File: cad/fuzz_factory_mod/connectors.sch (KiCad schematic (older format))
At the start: 6 parts

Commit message: Continued schematic
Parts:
- added R? (x2): 1M, symbol Device:R
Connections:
- net at K?.1 (+): now also D?.3 (common)
- net at K?.10 (R2): now also K?.3 (R1)
- net at K?.12 (-): now also D?.1 (A), Q?.3 (C)
- net AUDIO_OUT_CONN: now reaches K?.4 (C1)
- net AUDIO_OUT_CONN: now also R?.2
- net AUDIO_FX_OUT: now reaches K?.5 (T1)
- net AUDIO_FX_IN: now reaches K?.8 (T2)
- net AUDIO_IN_CONN: now reaches K?.9 (C2)
- net AUDIO_IN_CONN: now also R?.2
- net BYPASS_CMD: now reaches Q?.1 (B)
- net GNDPWR: now reaches Q?.2 (E)
- new net GNDA: R?.1, R?.1
- no-connect marks 0 -> 1
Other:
- moved on the sheet: D?, K?, Q?
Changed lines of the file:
@@
 $Descr A4 11693 8268
 encoding utf-8
-Sheet 4 5
+Sheet 5 6
 Title ""
 Date ""
@@
 L flax_lib:EE2-5NU K?
 U 1 1 5DE5A46A
-P 5550 3150
-F 0 "K?" H 5550 3681 50  0000 C CNN
-F 1 "EE2-5NU" H 5550 3590 50  0000 C CNN
-F 2 "" H 5550 3150 50  0000 C CNN
-F 3 "" H 5550 3150 50  0000 C CNN
-	1    5550 3150
+P 7900 4650
+F 0 "K?" H 7900 5181 50  0000 C CNN
+F 1 "EE2-5NU" H 7900 5090 50  0000 C CNN
+F 2 "" H 7900 4650 50  0000 C CNN
+F 3 "" H 7900 4650 50  0000 C CNN
+	1    7900 4650
 	1    0    0    -1
 $EndComp
@@
 L Transistor_BJT:DTC114Y Q?
 U 1 1 5DE5E2B7
-P 4800 4300
-F 0 "Q?" H 4988 4346 50  0000 L CNN
-F 1 "DTC114Y" H 4988 4255 50  0000 L CNN
-F 2 "" H 4800 4300 50  0001 L CNN
-F 3 "" H 4800 4300 50  0001 L CNN
-	1    4800 4300
+P 6400 5300
+F 0 "Q?" H 6588 5346 50  0000 L CNN
+F 1 "DTC114Y" H 6588 5255 50  0000 L CNN
+F 2 "" H 6400 5300 50  0001 L CNN
+F 3 "" H 6400 5300 50  0001 L CNN
+	1    6400 5300
 	1    0    0    -1
 $EndComp
@@
 L flax_lib:BAV23S D?
 U 1 1 5DE5F68B
-P 5850 4300
-F 0 "D?" V 5896 4379 50  0000 L CNN
-F 1 "BAV23S" V 5805 4379 50  0000 L CNN
-F 2 "" H 5850 4300 50  0001 C CNN
-F 3 "" H 5850 4300 50  0001 C CNN
-	1    5850 4300
-	0    -1   -1   0
+P 7400 5300
+F 0 "D?" V 7446 5379 50  0000 L CNN
+F 1 "BAV23S" V 7355 5379 50  0000 L CNN
+F 2 "" H 7400 5300 50  0001 C CNN
+F 3 "" H 7400 5300 50  0001 C CNN
+	1    7400 5300
+	1    0    0    1
 $EndComp
 $Comp
@@
 	1    0    0    -1
 $EndComp
+Wire Wire Line
+	8300 4600 8500 4600
+Wire Wire Line
+	8500 4600 8500 4300
+Wire Wire Line
+	8500 4300 8300 4300
+$Comp
+L power:GNDPWR #PWR?
+U 1 1 5E049671
+P 6500 5600
+F 0 "#PWR?" H 6500 5400 50  0001 C CNN
+F 1 "GNDPWR" H 6504 5446 50  0000 C CNN
+F 2 "" H 6500 5550 50  0001 C CNN
+F 3 "" H 6500 5550 50  0001 C CNN
+	1    6500 5600
+	1    0    0    -1
+$EndComp
+Wire Wire Line
+	6500 5500 6500 5600
+Wire Wire Line
+	6500 5000 6500 5100
+Wire Wire Line
+	6500 5000 7000 5000
+Wire Wire Line
+	7500 4900 7400 4900
+Wire Wire Line
+	7400 4900 7400 5100
+Wire Wire Line
+	7100 5300 7000 5300
+Wire Wire Line
+	7000 5300 7000 5000
+Connection ~ 7000 5000
+Wire Wire Line
+	7000 5000 7500 5000
+NoConn ~ 7700 5300
+Text HLabel 6000 5300 0    50   Input ~ 0
+BYPASS_CMD
+Wire Wire Line
+	6150 5300 6000 5300
+Text HLabel 7100 4400 0    50   Input ~ 0
+AUDIO_IN_CONN
+Text HLabel 7100 4700 0    50   Input ~ 0
+AUDIO_OUT_CONN
+$Comp
+L Device:R R?
+U 1 1 5E0563EF
+P 7400 4150
+F 0 "R?" H 7470 4196 50  0000 L CNN
+F 1 "1M" H 7470 4105 50  0000 L CNN
+F 2 "" V 7330 4150 50  0001 C CNN
+F 3 "~" H 7400 4150 50  0001 C CNN
+	1    7400 4150
+	1    0    0    -1
+$EndComp
+$Comp
+L Device:R R?
+U 1 1 5E056DB3
+P 7200 4150
+F 0 "R?" V 7300 4250 50  0000 R CNN
+F 1 "1M" V 7300 4100 50  0000 R CNN
+F 2 "" V 7130 4150 50  0001 C CNN
+F 3 "~" H 7200 4150 50  0001 C CNN
+	1    7200 4150
+	-1   0    0    -1
+$EndComp
+Wire Wire Line
+	7100 4400 7200 4400
+Wire Wire Line
+	7100 4700 7400 4700
+Wire Wire Line
+	7400 4300 7400 4700
+Connection ~ 7400 4700
+Wire Wire Line
+	7400 4700 7500 4700
+Wire Wire Line
+	7200 4300 7200 4400
+Connection ~ 7200 4400
+Wire Wire Line
+	7200 4400 7500 4400
+$Comp
+L power:GNDA #PWR?
+U 1 1 5E058766
+P 7400 3900
+F 0 "#PWR?" H 7400 3650 50  0001 C CNN
+F 1 "GNDA" H 7405 3727 50  0000 C CNN
+F 2 "" H 7400 3900 50  0001 C CNN
+F 3 "" H 7400 3900 50  0001 C CNN
+	1    7400 3900
+	-1   0    0    1
+$EndComp
+$Comp
+L power:GNDA #PWR?
+U 1 1 5E059243
+P 7200 3900
+F 0 "#PWR?" H 7200 3650 50  0001 C CNN
+F 1 "GNDA" H 7205 3727 50  0000 C CNN
+F 2 "" H 7200 3900 50  0001 C CNN
+F 3 "" H 7200 3900 50  0001 C CNN
+	1    7200 3900
+	-1   0    0    1
+$EndComp
+Wire Wire Line
+	7400 3900 7400 4000
+Wire Wire Line
+	7200 3900 7200 4000
+Text HLabel 8700 4500 2    50   Input ~ 0
+AUDIO_FX_IN
+Text HLabel 8700 4800 2    50   Input ~ 0
+AUDIO_FX_OUT
+Wire Wire Line
+	8700 4800 8300 4800
+Wire Wire Line
+	8300 4500 8700 4500
 $EndSCHEMATC

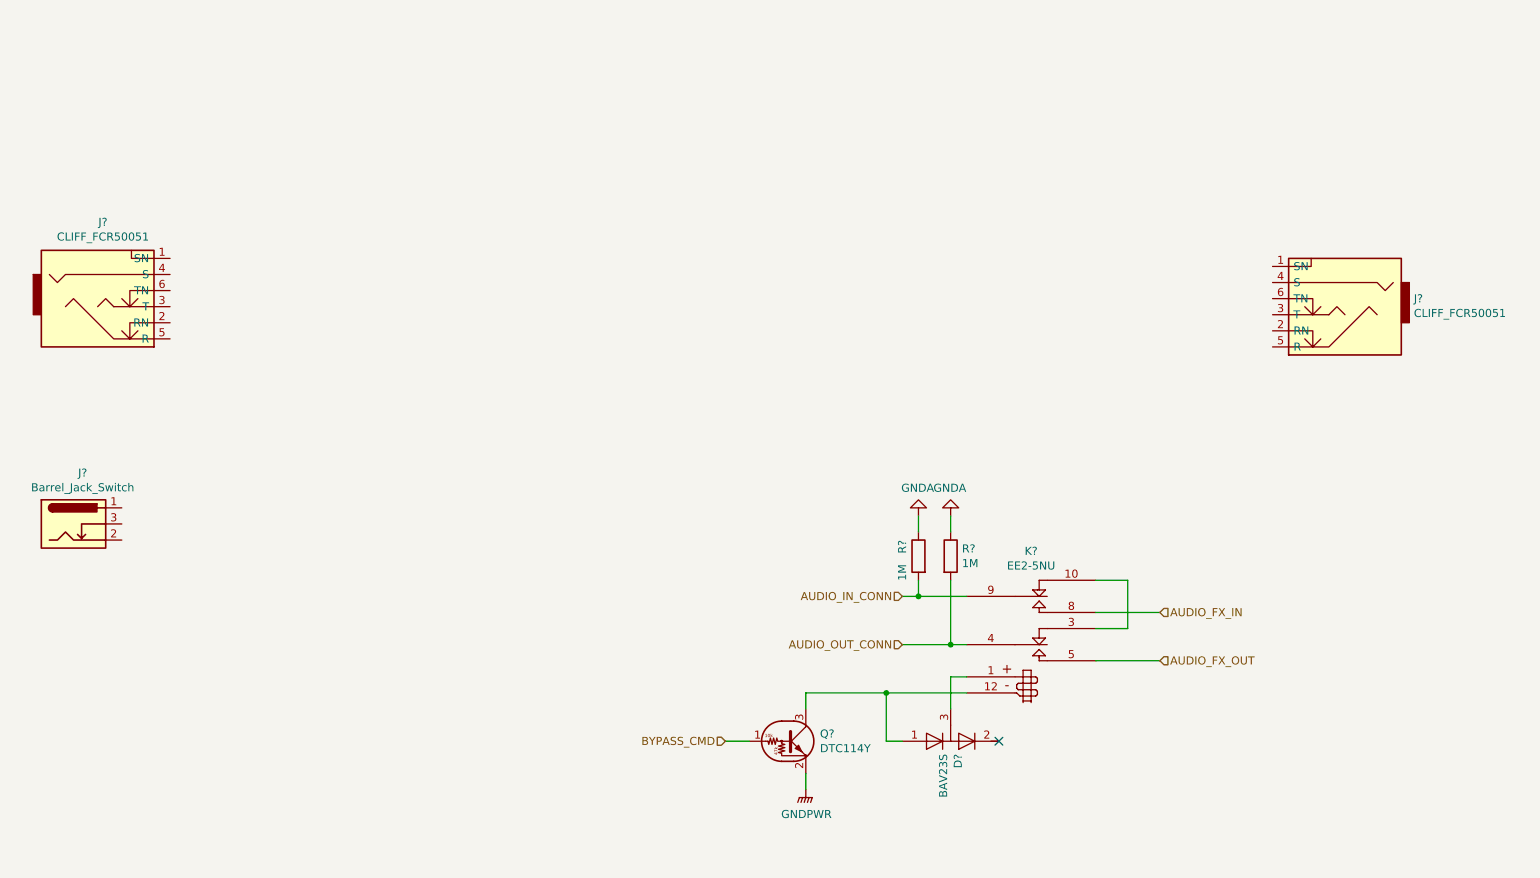
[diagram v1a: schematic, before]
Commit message: Continued schematic.
Added PSU and interface from tremolo project.
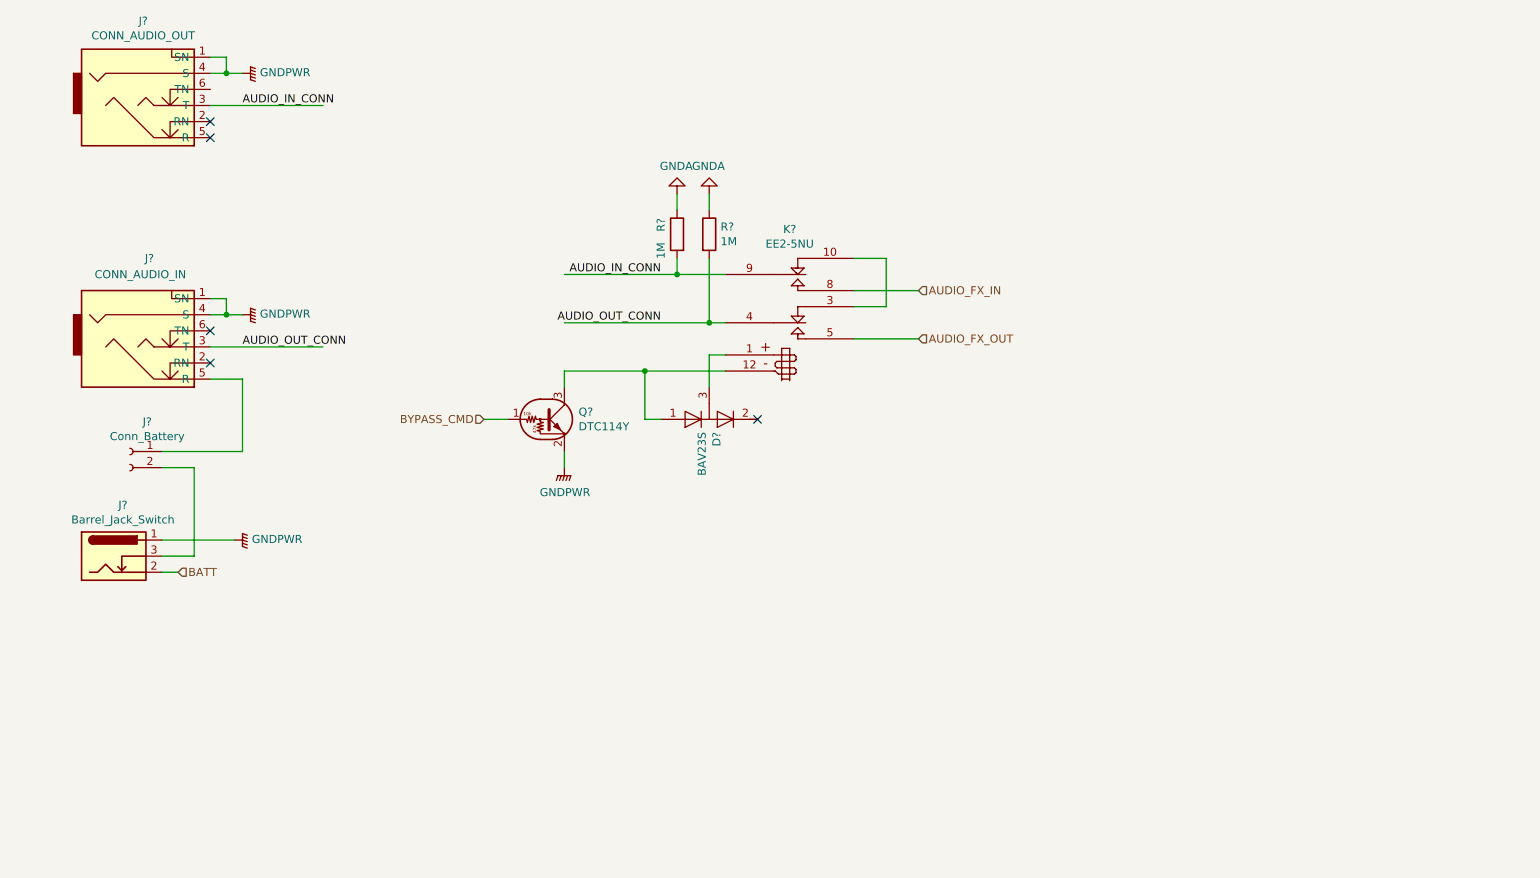
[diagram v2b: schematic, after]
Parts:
- added J?: Conn_Battery, symbol Connector:Conn_01x02_Female
- J?: value CLIFF_FCR50051 -> CONN_AUDIO_OUT
- J?: value CLIFF_FCR50051 -> CONN_AUDIO_IN
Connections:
- net labels added: BATT
- wire segments 22 -> 40
- no-connect marks 1 -> 5
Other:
- moved on the sheet: D?, J?, K?, Q?, R?

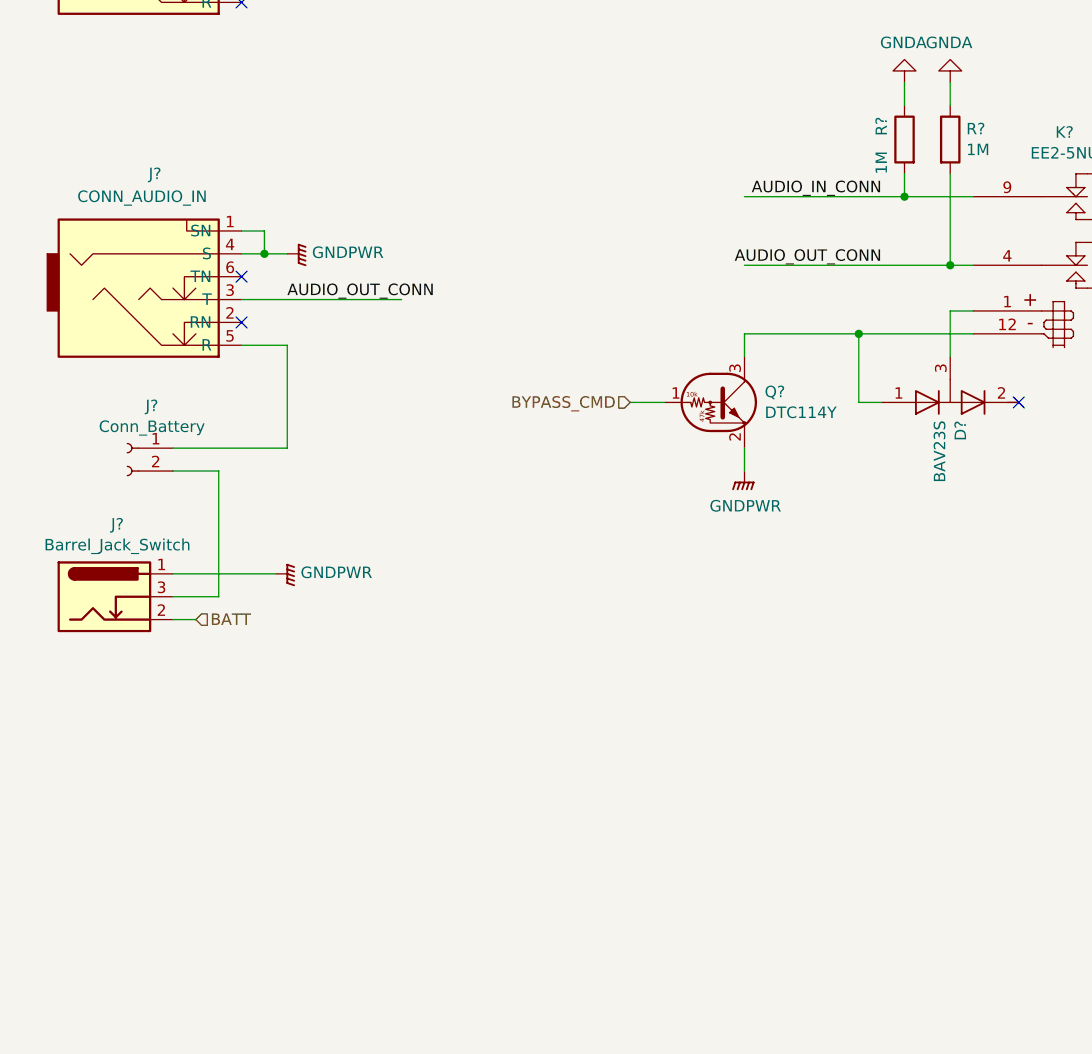
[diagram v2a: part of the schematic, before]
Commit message: Factorised fuzz factory circuit.
Added MIDI interface.
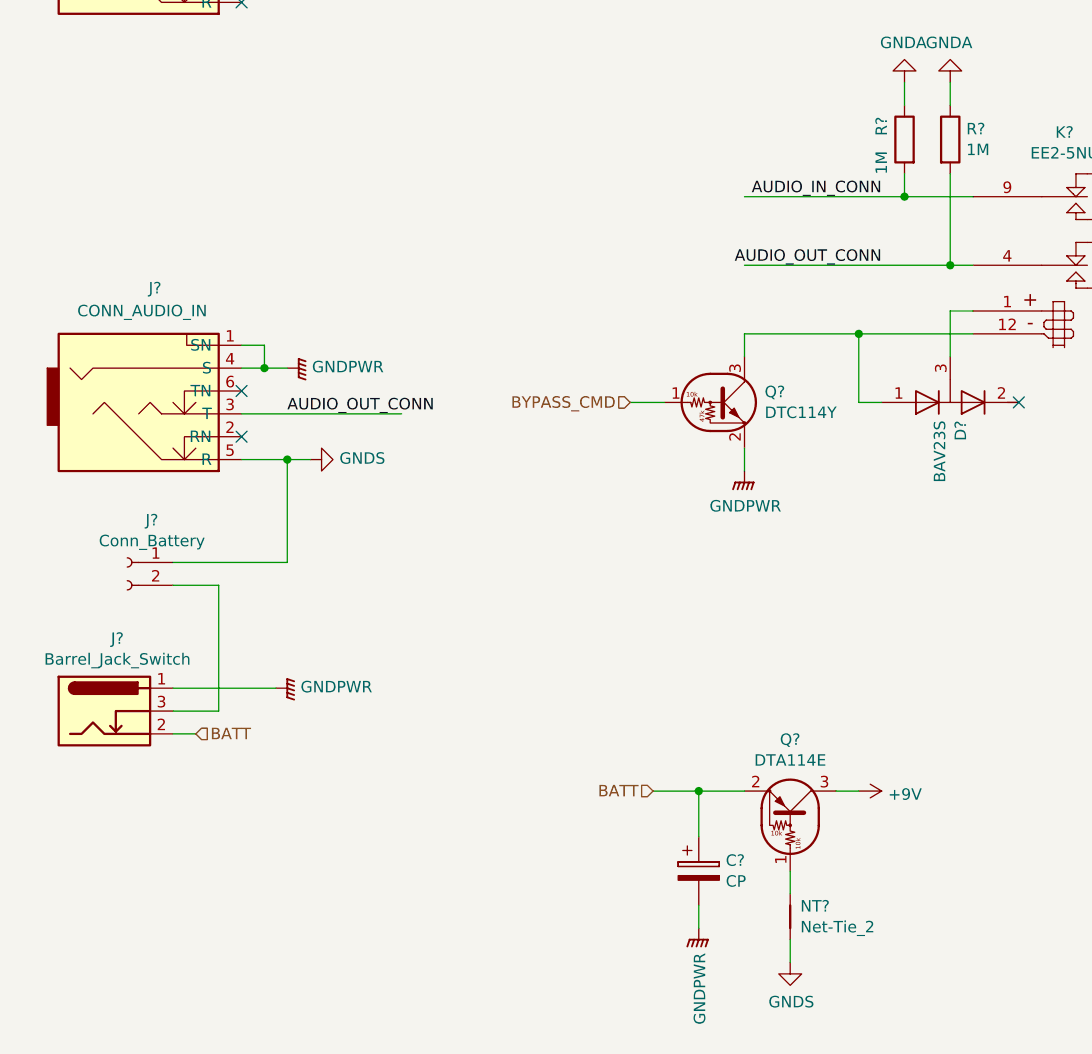
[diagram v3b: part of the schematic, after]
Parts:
- added C?: CP, symbol Device:CP
- added NT?: Net-Tie_2, symbol Device:Net-Tie_2
- added Q?: DTA114E, symbol Transistor_BJT:DTA114E
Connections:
- net labels added: +9V, GNDS
- wire segments 40 -> 48
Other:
- moved on the sheet: J?
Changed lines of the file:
@@
 $Descr A4 11693 8268
 encoding utf-8
-Sheet 6 11
+Sheet 7 14
 Title ""
 Date ""
@@
 L flax_lib:CLIFF_FCR50051 J?
 U 1 1 5DE5C90E
-P 2400 2850
-F 0 "J?" H 2450 3400 50  0000 R CNN
-F 1 "CONN_AUDIO_IN" H 2650 3300 50  0000 R CNN
-F 2 "" H 2500 2700 50  0001 C CNN
-F 3 "" H 2500 2700 50  0001 C CNN
-	1    2400 2850
+P 2400 3350
+F 0 "J?" H 2450 3900 50  0000 R CNN
+F 1 "CONN_AUDIO_IN" H 2650 3800 50  0000 R CNN
+F 2 "" H 2500 3200 50  0001 C CNN
+F 3 "" H 2500 3200 50  0001 C CNN
+	1    2400 3350
 	1    0    0    -1
 $EndComp
@@
 L Connector:Barrel_Jack_Switch J?
 U 1 1 5DE61D3B
-P 2200 4150
-F 0 "J?" H 2257 4467 50  0000 C CNN
-F 1 "Barrel_Jack_Switch" H 2257 4376 50  0000 C CNN
-F 2 "" H 2250 4110 50  0001 C CNN
-F 3 "~" H 2250 4110 50  0001 C CNN
-	1    2200 4150
+P 2200 4650
+F 0 "J?" H 2257 4967 50  0000 C CNN
+F 1 "Barrel_Jack_Switch" H 2257 4876 50  0000 C CNN
+F 2 "" H 2250 4610 50  0001 C CNN
+F 3 "~" H 2250 4610 50  0001 C CNN
+	1    2200 4650
 	1    0    0    -1
 $EndComp
@@
 Wire Wire Line
 	6800 2500 7200 2500
-Text HLabel 2600 4250 2    50   Input ~ 0
+Text HLabel 2600 4750 2    50   Input ~ 0
 BATT
 Wire Wire Line
-	2600 4250 2500 4250
+	2600 4750 2500 4750
 $Comp
 L power:GNDPWR #PWR?
 U 1 1 5E333C4B
-P 3000 2650
-F 0 "#PWR?" H 3000 2450 50  0001 C CNN
-F 1 "GNDPWR" V 3005 2542 50  0000 R CNN
-F 2 "" H 3000 2600 50  0001 C CNN
-F 3 "" H 3000 2600 50  0001 C CNN
-	1    3000 2650
+P 3000 3150
+F 0 "#PWR?" H 3000 2950 50  0001 C CNN
+F 1 "GNDPWR" V 3005 3042 50  0000 R CNN
+F 2 "" H 3000 3100 50  0001 C CNN
+F 3 "" H 3000 3100 50  0001 C CNN
+	1    3000 3150
 	0    -1   -1   0
 $EndComp
@@
 Wire Wire Line
 	2800 1350 3500 1350
-Text Label 3000 2850 0    50   ~ 0
+Text Label 3000 3350 0    50   ~ 0
 AUDIO_OUT_CONN
 Wire Wire Line
-	2800 2850 3500 2850
+	2800 3350 3500 3350
 $Comp
 L Connector:Conn_01x02_Female J?
 U 1 1 5E3469C4
-P 2300 3500
-F 0 "J?" H 2192 3685 50  0000 C CNN
-F 1 "Conn_Battery" H 2192 3594 50  0000 C CNN
-F 2 "" H 2300 3500 50  0001 C CNN
-F 3 "~" H 2300 3500 50  0001 C CNN
-	1    2300 3500
+P 2300 4000
+F 0 "J?" H 2192 4185 50  0000 C CNN
+F 1 "Conn_Battery" H 2192 4094 50  0000 C CNN
+F 2 "" H 2300 4000 50  0001 C CNN
+F 3 "~" H 2300 4000 50  0001 C CNN
+	1    2300 4000
 	-1   0    0    -1
 $EndComp
 Wire Wire Line
-	3000 3050 2800 3050
-NoConn ~ 2800 2950
-NoConn ~ 2800 2750
-Wire Wire Line
-	2800 2650 2900 2650
+	3000 3550 2800 3550
+NoConn ~ 2800 3450
+NoConn ~ 2800 3250
+Wire Wire Line
+	2800 3150 2900 3150
 $Comp
 L power:GNDPWR #PWR?
 U 1 1 5E34C9B1
-P 2950 4050
-F 0 "#PWR?" H 2950 3850 50  0001 C CNN
-F 1 "GNDPWR" V 2955 3942 50  0000 R CNN
-F 2 "" H 2950 4000 50  0001 C CNN
-F 3 "" H 2950 4000 50  0001 C CNN
-	1    2950 4050
+P 2950 4550
+F 0 "#PWR?" H 2950 4350 50  0001 C CNN
+F 1 "GNDPWR" V 2955 4442 50  0000 R CNN
+F 2 "" H 2950 4500 50  0001 C CNN
+F 3 "" H 2950 4500 50  0001 C CNN
+	1    2950 4550
 	0    -1   -1   0
 $EndComp
 Wire Wire Line
-	2500 4050 2950 4050
-Wire Wire Line
-	3000 3500 3000 3050
-Wire Wire Line
-	2500 3500 3000 3500
-Wire Wire Line
-	2500 4150 2700 4150
-Wire Wire Line
-	2700 4150 2700 3600
-Wire Wire Line
-	2700 3600 2500 3600
-Wire Wire Line
-	2800 2550 2900 2550
-Wire Wire Line
-	2900 2550 2900 2650
-Connection ~ 2900 2650
-Wire Wire Line
-	2900 2650 3000 2650
+	2500 4550 2950 4550
+Wire Wire Line
+	3000 4000 3000 3550
+Wire Wire Line
+	2500 4000 3000 4000
+Wire Wire Line
+	2500 4650 2700 4650
+Wire Wire Line
+	2700 4650 2700 4100
+Wire Wire Line
+	2700 4100 2500 4100
+Wire Wire Line
+	2800 3050 2900 3050
+Wire Wire Line
+	2900 3050 2900 3150
+Connection ~ 2900 3150
+Wire Wire Line
+	2900 3150 3000 3150
 $Comp
 L power:GNDPWR #PWR?
@@
 Wire Wire Line
 	5000 2400 5700 2400
+$Comp
+L Transistor_BJT:DTA114E Q?
+U 1 1 5E6CC80A
+P 5200 5100
+F 0 "Q?" V 5525 5100 50  0000 C CNN
+F 1 "DTA114E" V 5434 5100 50  0000 C CNN
+F 2 "" H 5200 5100 50  0001 L CNN
+F 3 "" H 5200 5100 50  0001 L CNN
+	1    5200 5100
+	0    1    -1   0
+$EndComp
+$Comp
+L Device:CP C?
+U 1 1 5E6D0A71
+P 4800 5350
+F 0 "C?" H 4918 5396 50  0000 L CNN
+F 1 "CP" H 4918 5305 50  0000 L CNN
+F 2 "" H 4838 5200 50  0001 C CNN
+F 3 "~" H 4800 5350 50  0001 C CNN
+	1    4800 5350
+	1    0    0    -1
+$EndComp
+Text HLabel 4600 5000 0    50   Input ~ 0
+BATT
+Wire Wire Line
+	5000 5000 4800 5000
+Wire Wire Line
+	4800 5200 4800 5000
+Connection ~ 4800 5000
+Wire Wire Line
+	4800 5000 4600 5000
+$Comp
+L power:GNDS #PWR?
+U 1 1 5E6D3A5E
+P 5200 5750
+F 0 "#PWR?" H 5200 5500 50  0001 C CNN
+F 1 "GNDS" H 5205 5577 50  0000 C CNN
+F 2 "" H 5200 5750 50  0001 C CNN
+F 3 "" H 5200 5750 50  0001 C CNN
+	1    5200 5750
+	1    0    0    -1
+$EndComp
+$Comp
+L power:GNDS #PWR?
+U 1 1 5E6D5175
+P 3100 3550
+F 0 "#PWR?" H 3100 3300 50  0001 C CNN
+F 1 "GNDS" V 3105 3422 50  0000 R CNN
+F 2 "" H 3100 3550 50  0001 C CNN
+F 3 "" H 3100 3550 50  0001 C CNN
+	1    3100 3550
+	0    -1   -1   0
+$EndComp
+Wire Wire Line
+	3100 3550 3000 3550
+Connection ~ 3000 3550
+$Comp
+L power:GNDPWR #PWR?
+U 1 1 5E6D6DCD
+P 4800 5600
+F 0 "#PWR?" H 4800 5400 50  0001 C CNN
+F 1 "GNDPWR" V 4805 5492 50  0000 R CNN
+F 2 "" H 4800 5550 50  0001 C CNN
+F 3 "" H 4800 5550 50  0001 C CNN
+	1    4800 5600
+	1    0    0    -1
+$EndComp
+Wire Wire Line
+	4800 5500 4800 5600
+$Comp
+L power:+9V #PWR?
+U 1 1 5E6D8A78
+P 5500 5000
+F 0 "#PWR?" H 5500 4850 50  0001 C CNN
+F 1 "+9V" V 5515 5128 50  0000 L CNN
+F 2 "" H 5500 5000 50  0001 C CNN
+F 3 "" H 5500 5000 50  0001 C CNN
+	1    5500 5000
+	0    1    1    0
+$EndComp
+Wire Wire Line
+	5500 5000 5400 5000
+$Comp
+L Device:Net-Tie_2 NT?
+U 1 1 5E6DBA2F
+P 5200 5550
+F 0 "NT?" V 5154 5594 50  0000 L CNN
+F 1 "Net-Tie_2" V 5245 5594 50  0000 L CNN
+F 2 "" H 5200 5550 50  0001 C CNN
+F 3 "~" H 5200 5550 50  0001 C CNN
+	1    5200 5550
+	0    1    1    0
+$EndComp
+Wire Wire Line
+	5200 5350 5200 5450
+Wire Wire Line
+	5200 5650 5200 5750
 $EndSCHEMATC
